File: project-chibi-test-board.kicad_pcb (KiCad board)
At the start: 2 copper layers, 221 parts, among them J1 Conn_01x04, J10 Conn_01x02, J11 Conn_01x02, J12 Conn_02x06_Top_Bottom, J13 Conn_02x06_Top_Bottom, J14 Conn_02x06_Top_Bottom, J15 Conn_02x06_Top_Bottom, J16 Conn_01x02, J17 Conn_01x02, J18 Conn_Coaxial, J19 Conn_Coaxial, J2 Conn_Coaxial, J20 Conn_01x03, J21 Conn_01x03, J22 Conn_01x04, J23 USB_B_Micro, J24 Conn_01x06, J25 Conn_01x04, J26 Conn_Coaxial, J27 Conn_Coaxial, J28 Conn_01x03, J29 Conn_01x03, J3 Conn_Coaxial, J30 Conn_01x02, J31 Conn_01x02, J32 Conn_02x06_Top_Bottom, J33 Conn_02x06_Top_Bottom, J34 Conn_02x06_Top_Bottom, J35 Conn_02x06_Top_Bottom, J36 Conn_02x06_Top_Bottom, J37 Conn_02x06_Top_Bottom, J38 Conn_02x06_Top_Bottom, J39 Conn_02x06_Top_Bottom, J4 Conn_01x03, J40 Conn_01x02, J41 Conn_01x02, J42 Conn_Coaxial, J43 Conn_Coaxial, J44 Conn_01x04, J45 Conn_01x03, J46 Conn_01x03, J47 Conn_01x06, J5 Conn_01x03, J6 Conn_02x06_Top_Bottom, J7 Conn_02x06_Top_Bottom, J8 Conn_02x06_Top_Bottom, J9 Conn_01x06, SW1 SW_DIP_x08, SW2 SW_DIP_x08, U1 40 MHz, U10 5M240ZT144C5N, U11 5M1270ZF256C5N, U2 2.048 MHz, U3 5M40ZE64C5N, U4 5M2210ZF256C5N, U5 93LC56BT-OT, U6 5M240ZT144C5N, U7 LM1117-3.3, U8 LM1117-1.8, U9 FT232H, Y1 12 MHz

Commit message: initial rough placement, too big physically
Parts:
- J30, J31, J40, J41: footprint Connector_PinSocket_2.54mm:PinSocket_1x02_P2.54mm_Vertical -> Connector_PinSocket_2.54mm:PinSocket_1x02_P2.54mm_Horizontal
- moved C27 211.1 mm to (263.7, 88.8)
- moved D8 211.1 mm to (259.4, 87.9)
- moved C20 211.1 mm to (271.4, 87.9)
- moved C26 211.1 mm to (261.8, 88.8)
- moved D5 211.1 mm to (275.3, 75.9)
- moved D7 211.1 mm to (275.3, 74.3)
- moved R10 211.1 mm to (275.2, 87.1)
- moved C15 211.1 mm to (274.7, 82.2)
- moved C17 211.1 mm to (274.7, 84.1)
- moved C18 211.1 mm to (274.7, 85.1)
- moved C19 211.1 mm to (269.5, 87.9)
- moved C21 211.1 mm to (273.3, 87.9)
- moved C24 211.1 mm to (274.7, 79.2)
- moved C25 211.1 mm to (274.7, 78.2)
- moved C28 211.1 mm to (274.7, 81.2)
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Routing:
- net Net-(D21-Pad2): track 0.00 -> 1.77 mm
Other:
- copper layers 2 -> 4
- net class Default: clearance 0.2 -> 0.1524; trace_width 0.25 -> 0.1524; via_dia 0.8 -> 0.6096; via_drill 0.4 -> 0.3048
- rule pad_to_mask_clearance: 0.2 -> 0.0762
- rule trace_clearance: 0.2 -> 0.1524
- rule trace_min: 0.2 -> 0.127
- rule via_min_drill: 0.3 -> 0.254
- rule via_min_size: 0.4 -> 0.4572

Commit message: more detailed placement
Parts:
- added MK1: Mounting_Hole, MountingHole:MountingHole_4mm, F.Cu at (55.9, 180.3)
- added MK2: Mounting_Hole, MountingHole:MountingHole_4mm, F.Cu at (55.9, 55.9)
- added MK3: Mounting_Hole, MountingHole:MountingHole_4mm, F.Cu at (149.9, 180.3)
- added MK4: Mounting_Hole, MountingHole:MountingHole_4mm, F.Cu at (149.9, 55.9)
- C10, C100, C101, C102, C103, C104, C11, C12, C13, C14, C15, C16, C17, C18, C19, C20, C21, C22, C23, C24, C25, C26, C27, C28, C29, C3, C30, C31, C32, C33, C34, C37, C38, C39, C4, C45, C49, C5, C50, C51, C52, C54, C55, C56, C57, C58, C59, C6, C60, C61, C62, C63, C64, C65, C66, C67, C68, C69, C7, C70, C71, C72, C73, C74, C75, C76, C77, C78, C79, C8, C80, C81, C82, C83, C84, C85, C86, C87, C88, C89, C9, C90, C91, C92, C93, C94, C95, C96, C97, C98, C99: moved to B.Cu
- C48: footprint Capacitor_SMD:C_0402_1005Metric -> Capacitor_SMD:C_0603_1608Metric
- moved R2 167.0 mm to (99.4, 121.2), turned to 180 degrees
- moved U2 166.5 mm to (100.0, 123.4), turned to 180 degrees
- moved R1 163.2 mm to (101.3, 121.2), turned to 180 degrees
- moved C1 159.4 mm to (103.2, 121.2), turned to 180 degrees
- moved U1 158.5 mm to (104.0, 123.4), turned to 180 degrees
- moved C2 155.6 mm to (105.1, 121.2), turned to 180 degrees
- moved C18 152.6 mm to (123.0, 69.0)
- moved C25 151.8 mm to (123.0, 84.0), turned to 180 degrees
- moved C68 150.5 mm to (73.0, 166.5), turned to 180 degrees
- moved C76 148.3 mm to (78.0, 166.5), turned to 180 degrees
- moved C69 148.3 mm to (69.5, 162.5), turned to 90 degrees
- moved C28 147.3 mm to (127.5, 76.0)
- moved C16 146.8 mm to (128.2, 74.3), turned to 225 degrees
- moved C24 146.6 mm to (128.2, 78.7), turned to 135 degrees
- moved D5 145.6 mm to (130.6, 91.7), turned to 90 degrees
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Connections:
- C31 pad 1: +3V3 -> +1V8
- C32 pad 1: +3V3 -> +1V8
- C33 pad 1: +3V3 -> +1V8
- C34 pad 1: +3V3 -> +1V8
- U4 pad F10: +3V3 -> +1V8
- U4 pad G11: +3V3 -> +1V8
- U4 pad H10: +3V3 -> +1V8
- U4 pad H8: +3V3 -> +1V8
- U4 pad J7: +3V3 -> +1V8
- U4 pad J9: +3V3 -> +1V8
- U4 pad K6: +3V3 -> +1V8
- U4 pad L7: +3V3 -> +1V8
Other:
- board outline added: 104.1 x 134.6 mm

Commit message: misc
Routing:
- added copper zone on In1.Cu, net GND
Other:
- board text added: "1"
- board text added: "2"
- board text added: "3"
- board text added: "4"
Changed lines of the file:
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@@
   (general
     (thickness 1.6)
-    (drawings 22)
+    (drawings 26)
     (tracks 1)
     (zones 0)
@@
     (45 Margin user)
     (46 B.CrtYd user)
-    (47 F.CrtYd user hide)
+    (47 F.CrtYd user)
     (48 B.Fab user)
-    (49 F.Fab user hide)
+    (49 F.Fab user)
   )
   (setup
     (last_trace_width 0.1524)
     (trace_clearance 0.1524)
-    (zone_clearance 0.508)
+    (zone_clearance 0.254)
     (zone_45_only no)
     (trace_min 0.127)
@@
       (net 1 "Net-(J23-Pad1)"))
   )
+  (gr_text 4 (at 55.88 174.625) (layer B.Cu)
+    (effects (font (size 1.524 1.524) (thickness 0.1524)))
+  )
+  (gr_text 3 (at 54.61 174.625) (layer In2.Cu)
+    (effects (font (size 1.524 1.524) (thickness 0.1524)))
+  )
+  (gr_text 2 (at 53.34 174.625) (layer In1.Cu)
+    (effects (font (size 1.524 1.524) (thickness 0.1524)))
+  )
+  (gr_text 1 (at 52.07 174.625) (layer F.Cu)
+    (effects (font (size 1.524 1.524) (thickness 0.1524)))
+  )
   (dimension 67.31 (width 0.3) (layer Cmts.User)
     (gr_text "2.6500 in" (at 37.27 151.765 270) (layer Cmts.User)
@@
   (gr_line (start 50.8 50.8) (end 50.8 185.42) (layer Edge.Cuts) (width 0.15))
   (segment (start 116.405001 151.429999) (end 116.405001 149.659999) (width 0.1524) (layer B.Cu) (net 81))
+  (zone (net 5) (net_name GND) (layer In1.Cu) (hatch edge 0.508)
+    (connect_pads (clearance 0.254))
+    (min_thickness 0.254)
+    (fill yes (arc_segments 16) (thermal_gap 0.508) (thermal_bridge_width 0.508))
+    (polygon
+      (pts
+        (xy 154.305 184.785) (xy 154.305 51.435) (xy 51.435 51.435) (xy 51.435 184.785)
+      )
+    )
+  )
 )

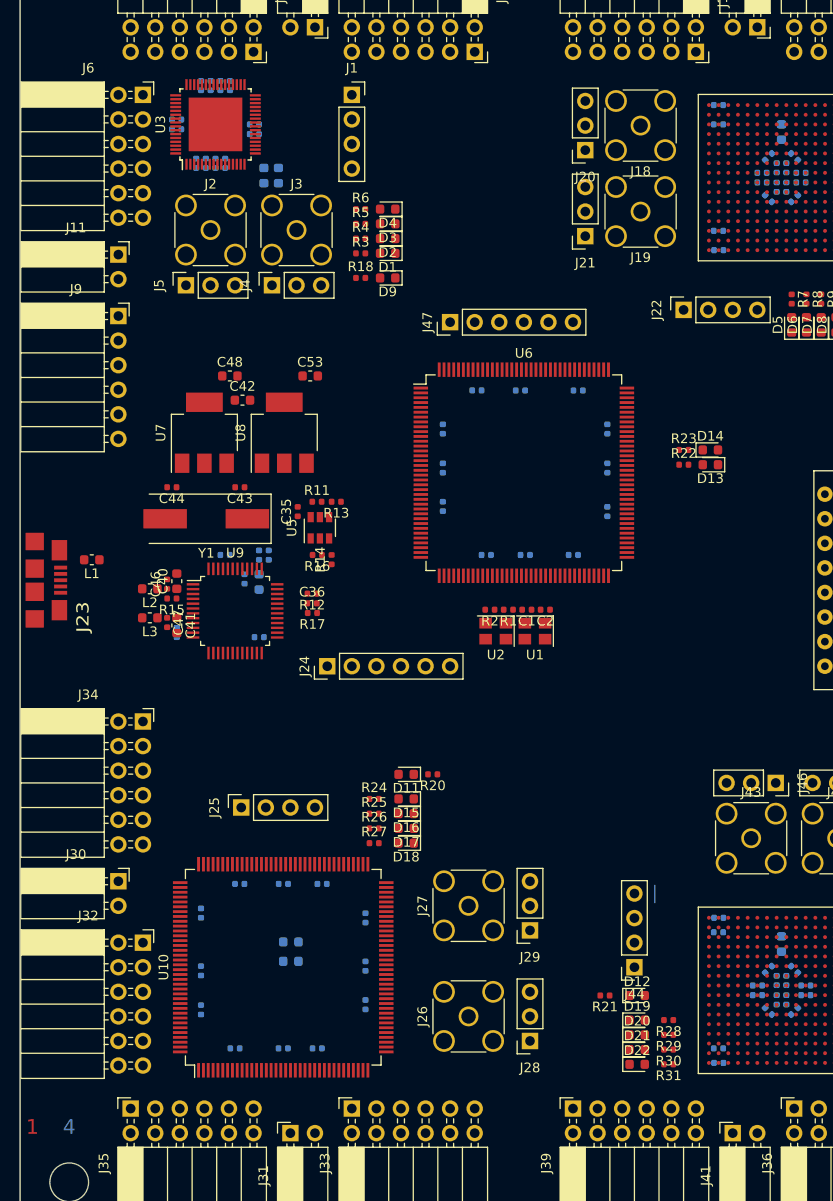
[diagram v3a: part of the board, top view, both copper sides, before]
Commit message: first order  approximation of planes
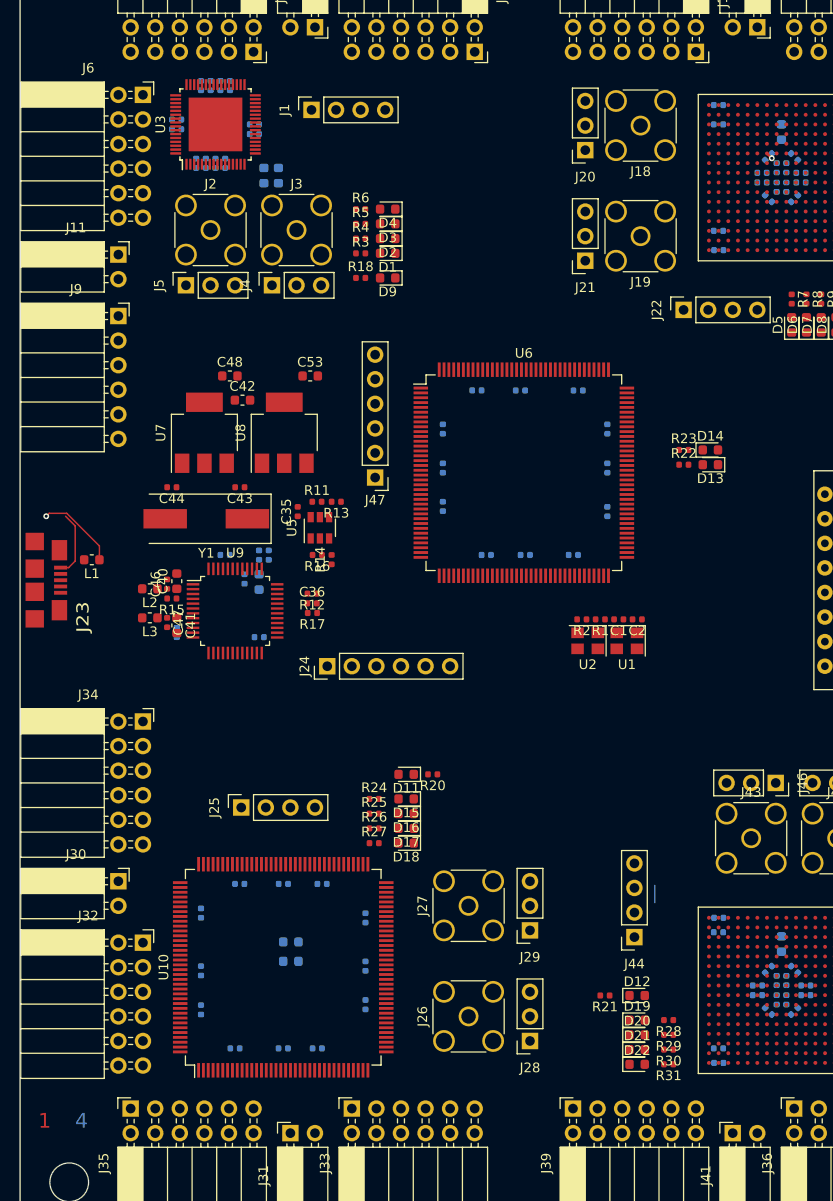
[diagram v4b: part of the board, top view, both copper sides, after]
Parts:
- moved J47 17.8 mm to (87.5, 107.5), turned to 180 degrees
- moved C1 9.55 mm to (112.7, 122.2)
- moved C2 9.55 mm to (114.6, 122.2)
- moved R1 9.55 mm to (110.8, 122.2)
- moved R2 9.55 mm to (108.9, 122.2)
- moved U1 9.55 mm to (113.5, 124.4)
- moved U2 9.55 mm to (109.5, 124.4)
- moved J1 4.45 mm to (80.9, 69.5), turned to 90 degrees
- moved J44 3.12 mm to (114.3, 155.0)
- moved J21 2.54 mm to (109.2, 85.1)
- moved J19 2.54 mm to (114.9, 82.5)
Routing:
- net +5V: track 0.00 -> 547.1 mm, vias 0 -> 1
- net Net-(J23-Pad1): track 0.00 -> 6.83 mm
- net +1V8: track 0.00 -> 0.71 mm, vias 0 -> 1
- added copper zone on In2.Cu, net +1V8
- added copper zone on In2.Cu, net +3V3
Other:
- net class Power added: clearance 0.1524, trace_width 0.254, via_dia 0.6096, via_drill 0.3048

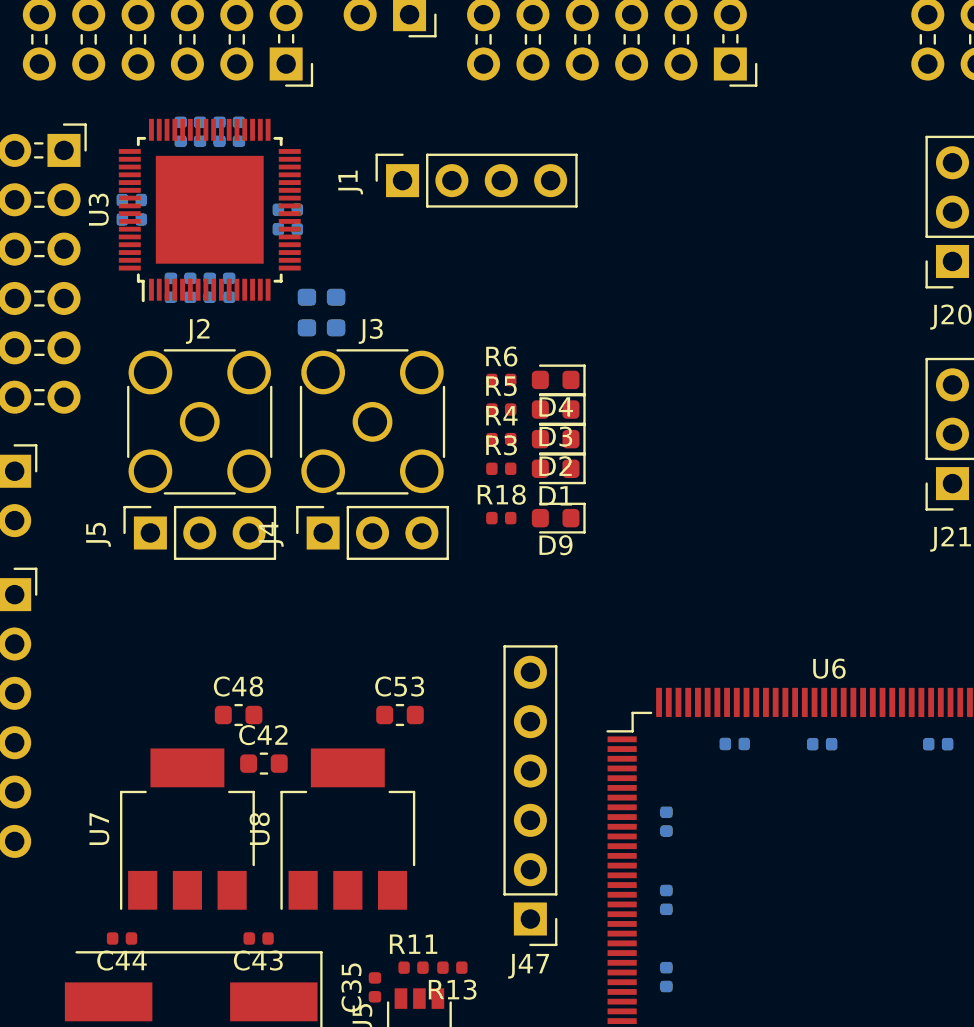
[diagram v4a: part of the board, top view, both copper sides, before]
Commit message: delete excess caps for 40z; add bulk for mux
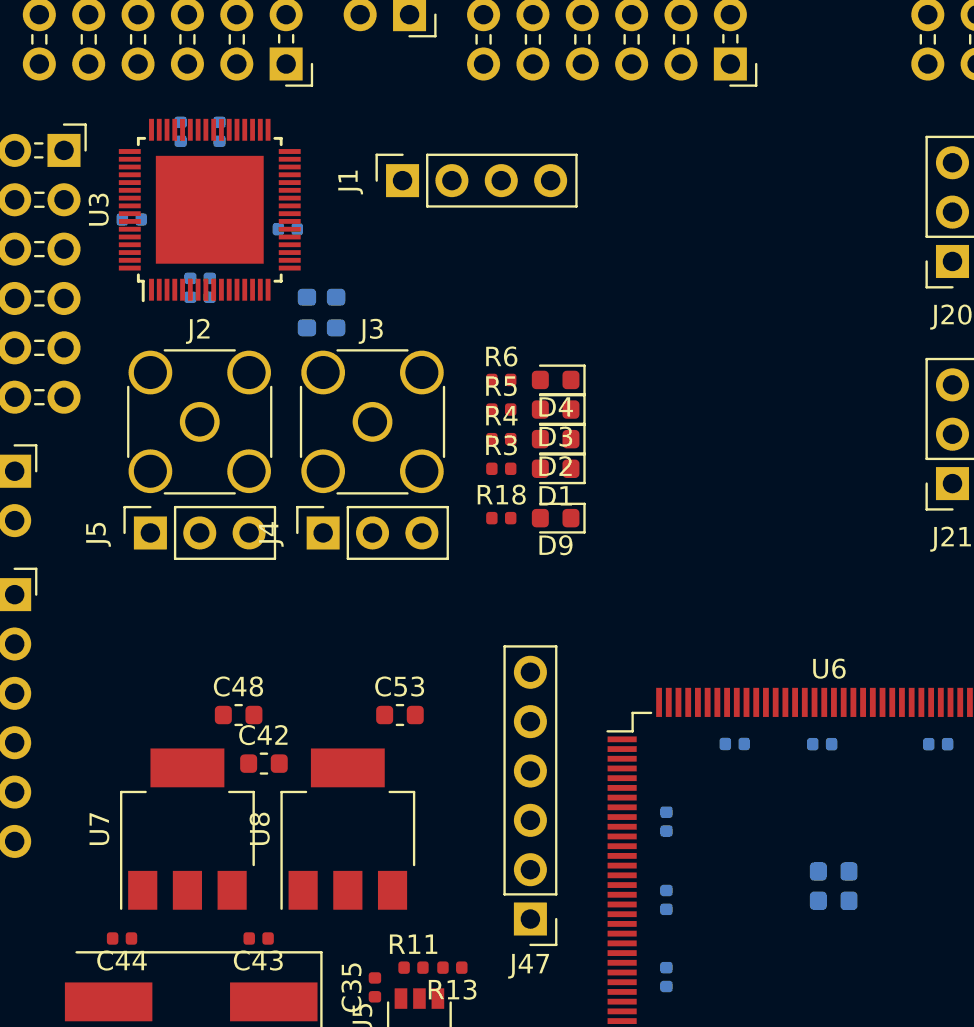
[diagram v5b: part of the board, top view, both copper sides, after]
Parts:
- removed C13, C14, C5, C6: 0.1 uF, Capacitor_SMD:C_0402_1005Metric
- C3, C4: value 0.1 uF -> 4.7 uF; footprint Capacitor_SMD:C_0402_1005Metric -> Capacitor_SMD:C_0603_1608Metric
- moved C3 50.0 mm to (103.1, 105.0)
- moved C4 46.5 mm to (103.1, 106.6), turned to 0 degrees
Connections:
- C3 pad 1: +3V3 -> +1V8
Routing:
- net +5V: track 547.1 -> 547.9 mm
